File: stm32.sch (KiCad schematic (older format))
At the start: 29 parts, among them J6 USB_C_Receptacle_USB2.0, U3 STM32F205RBTx, U4 OLED_0.96\"_SSD1306, Y2 8M

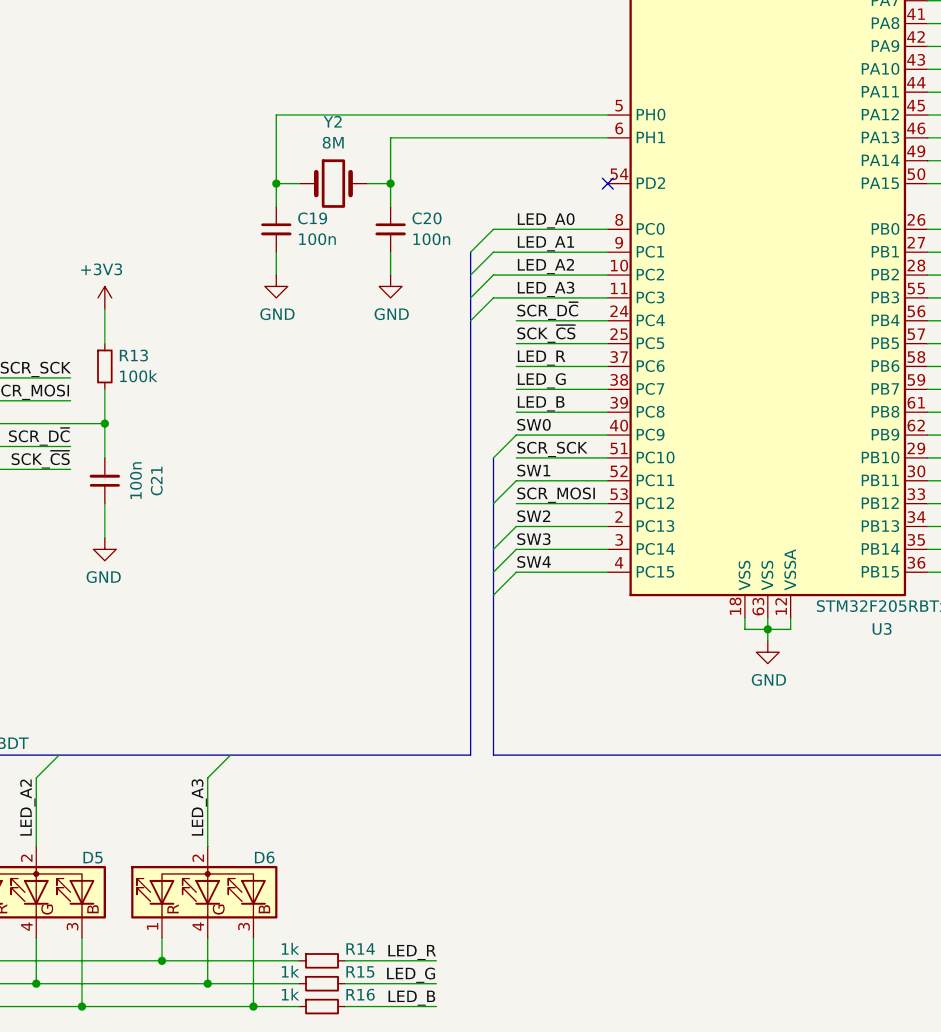
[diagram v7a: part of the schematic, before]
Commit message: sch, pcb: Add a 5th RGB LED
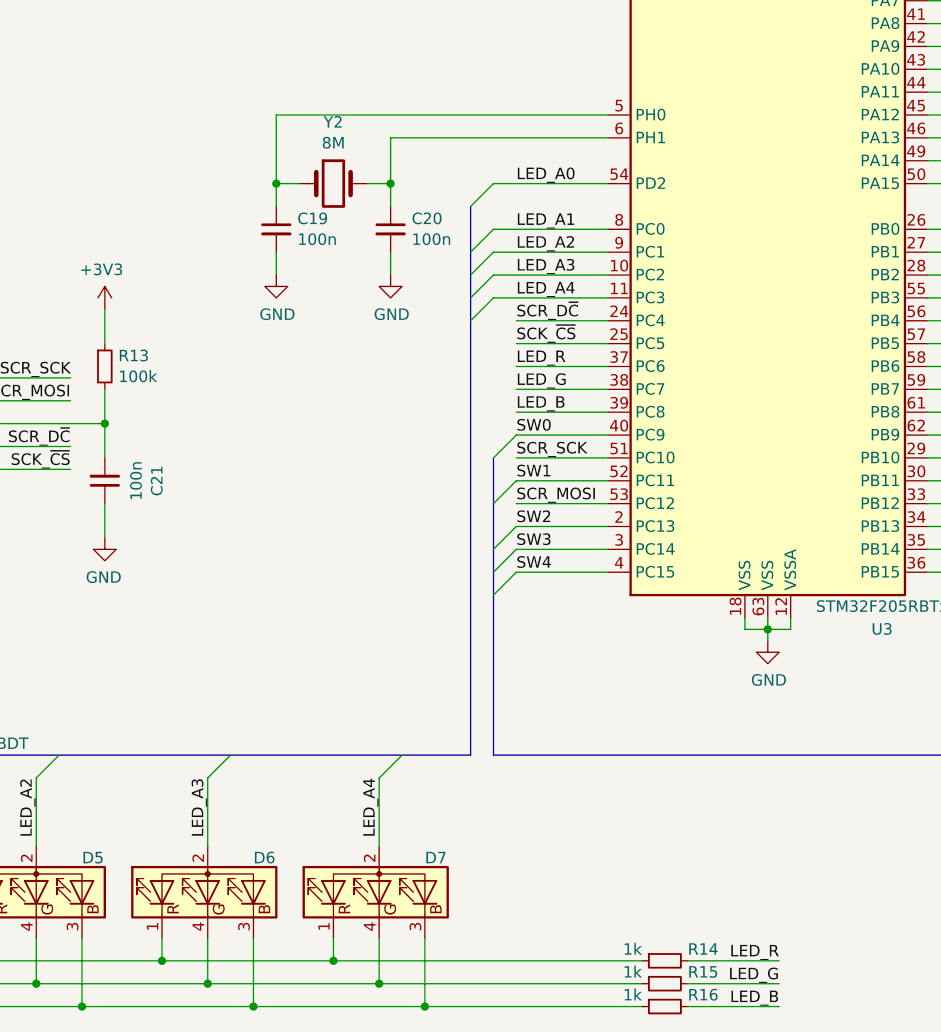
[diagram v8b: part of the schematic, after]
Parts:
- added D7: MHPA1515RGBDT, antboard:PLCC1515, symbol Device:LED_RABG
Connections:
- net LED_A0: now also U3.54 (PD2); no longer U3.8 (PC0)
- net LED_A1: now also U3.8 (PC0); no longer U3.9 (PC1)
- net LED_A2: now also U3.9 (PC1); no longer U3.10 (PC2)
- net LED_A3: now also U3.10 (PC2); no longer U3.11 (PC3)
- net at D3.1 (RK), D4.1 (RK), D5.1 (RK)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: now also D7.1 (RK)
- net at D3.4 (GK), D4.4 (GK), D5.4 (GK)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: now also D7.4 (GK)
- net at D3.3 (BK), D4.3 (BK), D5.3 (BK)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: now also D7.3 (BK)
- new net LED_A4: D7.2 (A), U3.11 (PC3)
- no-connect marks 5 -> 4
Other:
- moved on the sheet: R14, R15, R16
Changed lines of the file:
@@
 Text Label 4600 4950 0    50   ~ 0
 LED_B
+Text Label 4600 3950 0    50   ~ 0
+LED_A0
 Text Label 4600 4150 0    50   ~ 0
-LED_A0
+LED_A1
 Text Label 4600 4250 0    50   ~ 0
-LED_A1
+LED_A2
 Text Label 4600 4350 0    50   ~ 0
-LED_A2
-Text Label 4600 4450 0    50   ~ 0
 LED_A3
 Connection ~ 2700 7550
@@
 	2700 7550 3450 7550
 Wire Wire Line
-	3650 7350 3050 7350
+	5150 7350 3800 7350
 Connection ~ 3050 7350
 Wire Wire Line
-	3250 7450 3650 7450
+	3250 7450 4000 7450
 Connection ~ 3250 7450
 Wire Wire Line
-	3650 7550 3450 7550
+	5150 7550 4200 7550
 Connection ~ 3450 7550
 Entry Wire Line
@@
 	4400 4550 4500 4450
 Wire Wire Line
+	4500 3950 5000 3950
+Wire Wire Line
 	4500 4150 5000 4150
 Wire Wire Line
@@
 Wire Wire Line
 	4500 4350 5000 4350
-Wire Wire Line
-	4500 4450 5000 4450
 Wire Wire Line
 	5000 5150 4600 5150
@@
 SCK_~CS
 Wire Wire Line
-	3850 7350 4250 7350
-Text Label 4250 7350 2    50   ~ 0
+	5350 7350 5750 7350
+Text Label 5750 7350 2    50   ~ 0
 LED_R
 Wire Wire Line
-	3850 7450 4250 7450
-Text Label 4250 7450 2    50   ~ 0
+	5350 7450 5750 7450
+Text Label 5750 7450 2    50   ~ 0
 LED_G
 Wire Wire Line
-	3850 7550 4250 7550
-Text Label 4250 7550 2    50   ~ 0
+	5350 7550 5750 7550
+Text Label 5750 7550 2    50   ~ 0
 LED_B
 $Comp
 L Device:R_Small R?
 U 1 1 5E2945B4
-P 3750 7350
+P 5250 7350
 AR Path="/5DF7E971/5E2945B4" Ref="R?"  Part="1"
 AR Path="/5DFC2583/5E2945B4" Ref="R14"  Part="1"
-F 0 "R14" V 3700 7250 50  0000 R CNN
-F 1 "1k" V 3700 7450 50  0000 L CNN
-F 2 "Resistor_SMD:R_0603_1608Metric" H 3750 7350 50  0001 C CNN
-F 3 "~" H 3750 7350 50  0001 C CNN
-	1    3750 7350
+F 0 "R14" V 5200 7250 50  0000 R CNN
+F 1 "1k" V 5200 7450 50  0000 L CNN
+F 2 "Resistor_SMD:R_0603_1608Metric" H 5250 7350 50  0001 C CNN
+F 3 "~" H 5250 7350 50  0001 C CNN
+	1    5250 7350
 	0    -1   1    0
 $EndComp
@@
 L Device:R_Small R?
 U 1 1 5E295ACD
-P 3750 7450
+P 5250 7450
 AR Path="/5DF7E971/5E295ACD" Ref="R?"  Part="1"
 AR Path="/5DFC2583/5E295ACD" Ref="R15"  Part="1"
-F 0 "R15" V 3700 7350 50  0000 R CNN
-F 1 "1k" V 3700 7550 50  0000 L CNN
-F 2 "Resistor_SMD:R_0603_1608Metric" H 3750 7450 50  0001 C CNN
-F 3 "~" H 3750 7450 50  0001 C CNN
-	1    3750 7450
+F 0 "R15" V 5200 7350 50  0000 R CNN
+F 1 "1k" V 5200 7550 50  0000 L CNN
+F 2 "Resistor_SMD:R_0603_1608Metric" H 5250 7450 50  0001 C CNN
+F 3 "~" H 5250 7450 50  0001 C CNN
+	1    5250 7450
 	0    -1   1    0
 $EndComp
@@
 L Device:R_Small R?
 U 1 1 5E295D66
-P 3750 7550
+P 5250 7550
 AR Path="/5DF7E971/5E295D66" Ref="R?"  Part="1"
 AR Path="/5DFC2583/5E295D66" Ref="R16"  Part="1"
-F 0 "R16" V 3700 7450 50  0000 R CNN
-F 1 "1k" V 3700 7650 50  0000 L CNN
-F 2 "Resistor_SMD:R_0603_1608Metric" H 3750 7550 50  0001 C CNN
-F 3 "~" H 3750 7550 50  0001 C CNN
-	1    3750 7550
+F 0 "R16" V 5200 7450 50  0000 R CNN
+F 1 "1k" V 5200 7650 50  0000 L CNN
+F 2 "Resistor_SMD:R_0603_1608Metric" H 5250 7550 50  0001 C CNN
+F 3 "~" H 5250 7550 50  0001 C CNN
+	1    5250 7550
 	0    -1   1    0
 $EndComp
@@
 Wire Wire Line
 	1850 5400 1850 5500
-NoConn ~ 5000 3950
 Wire Wire Line
 	1350 1900 1900 1900
@@
 Text Label 6800 3950 2    50   ~ 0
 ADC_RDY
-Wire Bus Line
-	4400 4250 4400 6450
-Wire Bus Line
-	1100 6450 4400 6450
-Wire Bus Line
-	4500 5150 4500 6450
-Wire Bus Line
-	8300 5250 8300 6450
 $Comp
 L Device:LED_RABG D3
@@
 	0    -1   -1   0
 $EndComp
+Wire Wire Line
+	4000 7450 4000 7250
+Wire Wire Line
+	3800 7350 3800 7250
+Entry Wire Line
+	4000 6550 4100 6450
+Text Label 4000 6550 3    50   ~ 0
+LED_A4
+Wire Wire Line
+	4000 6850 4000 6550
+Wire Wire Line
+	4200 7250 4200 7550
+$Comp
+L Device:LED_RABG D7
+U 1 1 5E30E6A1
+P 4000 7050
+F 0 "D7" V 4150 6850 50  0000 R CNN
+F 1 "MHPA1515RGBDT" V 3955 6720 50  0001 R CNN
+F 2 "antboard:PLCC1515" H 4000 7000 50  0001 C CNN
+F 3 "~" H 4000 7000 50  0001 C CNN
+	1    4000 7050
+	0    -1   -1   0
+$EndComp
+Connection ~ 3800 7350
+Wire Wire Line
+	3800 7350 3050 7350
+Connection ~ 4000 7450
+Wire Wire Line
+	4000 7450 5150 7450
+Connection ~ 4200 7550
+Wire Wire Line
+	4200 7550 3450 7550
+Text Label 4600 4450 0    50   ~ 0
+LED_A4
+Wire Wire Line
+	4500 4450 5000 4450
+Entry Wire Line
+	4400 4050 4500 3950
+Wire Bus Line
+	4400 4050 4400 6450
+Wire Bus Line
+	1100 6450 4400 6450
+Wire Bus Line
+	4500 5150 4500 6450
+Wire Bus Line
+	8300 5250 8300 6450
 $EndSCHEMATC
